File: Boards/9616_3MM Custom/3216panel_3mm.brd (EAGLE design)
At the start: 384.8 x 81.3 mm, 452 parts, among them U1 74HC164D, U10 74HCT04D, U11 HT1632C, U12 HT1632C, U13 74HC164D, U14 HT1632C, U15 HT1632C, U16 74HCT04D, U17 HT1632C, U18 HT1632C, U2 HT1632C, U3 HT1632C, U4 74HCT04D, U5 HT1632C, U6 HT1632C, U7 74HC164D, U8 HT1632C, U9 HT1632C

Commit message: Finished routing board (for Sierra Circuits/PCBCart.com specs)
Signed-off-by: Evan Richardson <erichardson@savi.com>
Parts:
- C1, C2: value 10pf -> 10pF
- moved C5 8.89 mm to (44.2, -14.0)
- moved U6 7.62 mm to (56.7, -16.0)
- moved BR1 7.17 mm to (27.2, -14.7)
- moved R268 0.51 mm to (290.1, 7.62)
- moved R293 0.25 mm to (275.8, -7.62)
- moved R273 0.13 mm to (275.9, 7.62)
- moved R276 0.13 mm to (260.6, 7.62)
- moved R100 0.07 mm to (2.02, -24.1)
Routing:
- net +5V: track 0.00 -> 1258.6 mm, vias 0 -> 22
- net GND: track 0.00 -> 1226.7 mm, vias 0 -> 36
- net WR_A_OUT: track 0.00 -> 352.8 mm, vias 0 -> 7
- net DATA_A_OUT: track 0.00 -> 333.3 mm, vias 0 -> 10
- net WR_B_OUT: track 0.00 -> 305.6 mm, vias 0 -> 9
- net DATA_B_OUT: track 0.00 -> 288.7 mm, vias 0 -> 6
- net CS4: track 0.00 -> 223.0 mm, vias 0 -> 3
- net CSB_4: track 0.00 -> 198.7 mm, vias 0 -> 2
- net CLK_A_OUT: track 0.00 -> 192.3 mm, vias 0 -> 3
- net CLK_B_OUT: track 0.00 -> 178.3 mm, vias 0 -> 4
- net DATA_C_OUT: track 0.00 -> 160.4 mm, vias 0 -> 4
- net WR_C_OUT: track 0.00 -> 154.7 mm, vias 0 -> 7
- net ANODE_J4: track 0.00 -> 124.9 mm, vias 0 -> 1
- net ANODE_D6: track 0.00 -> 109.8 mm, vias 0 -> 1
- net CATHODE_F23: track 0.00 -> 101.9 mm, vias 0 -> 1
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- added copper zone on layer 1, net GND
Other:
- board size 384.8 x 81.3 mm -> 384.5 x 81.3 mm

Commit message: added fiducial marks increased 5V supply to 16mil
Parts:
- added JP1, JP2, JP3, JP4: FIDUCIAL1X2.5, SparkFun-Aesthetics:FIDUCIAL-1X2.5
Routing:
- net CATHODE_A10: track 28.3 -> 29.5 mm
- net CATHODE_A23: track 38.0 -> 39.1 mm
- net CATHODE_J16: track 44.9 -> 45.9 mm
- net CATHODE_A11: track 32.9 -> 33.9 mm
- added copper zone on layer 1, net +5V
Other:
- board size 384.5 x 81.3 mm -> 384.8 x 81.3 mm

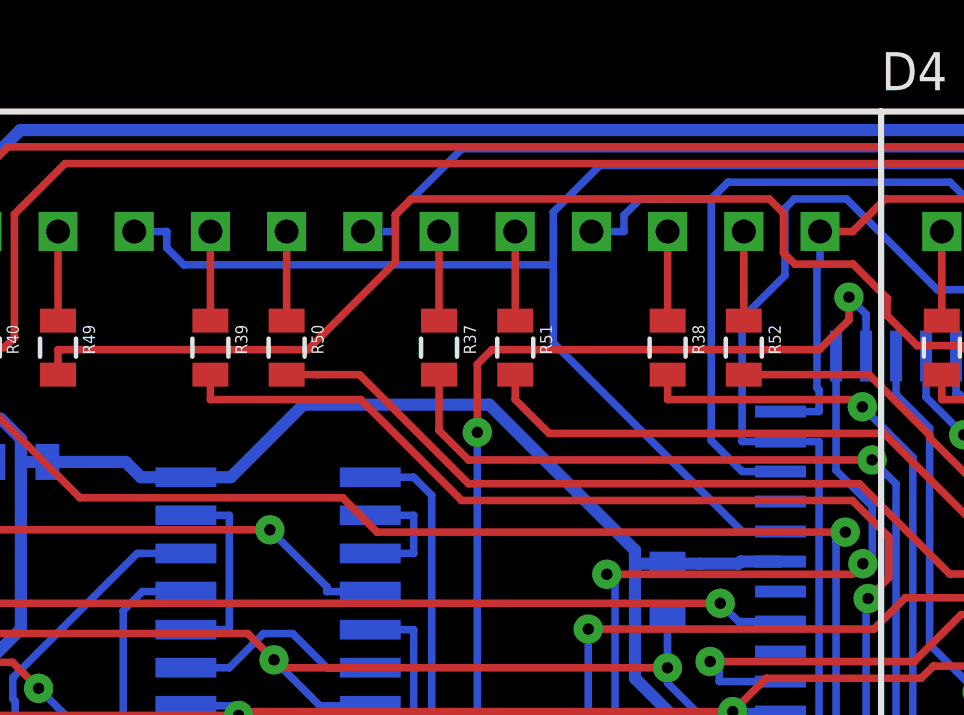
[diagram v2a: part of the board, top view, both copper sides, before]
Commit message: fixed missing connection on pin 19 of 3rd/4th top displays on left side of Boards/9616_3MM Custom/3216panel_3mm.brd
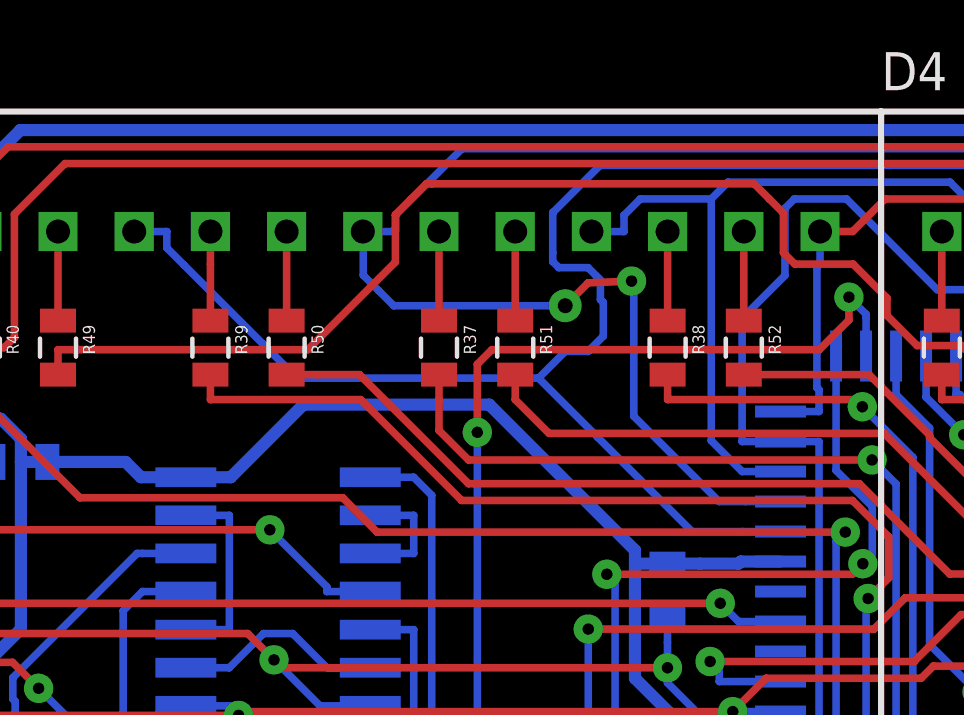
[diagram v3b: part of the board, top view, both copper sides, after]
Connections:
- net ANODE_B1: now also U2.23
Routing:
- net ANODE_B1: track 34.9 -> 56.7 mm, vias 0 -> 2
- net ANODE_B0: track 49.2 -> 54.1 mm
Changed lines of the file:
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@@
 <layer number="17" name="Pads" color="2" fill="1" visible="yes" active="yes"/>
 <layer number="18" name="Vias" color="2" fill="1" visible="yes" active="yes"/>
-<layer number="19" name="Unrouted" color="6" fill="1" visible="yes" active="yes"/>
+<layer number="19" name="Unrouted" color="17" fill="1" visible="yes" active="yes"/>
 <layer number="20" name="Dimension" color="15" fill="1" visible="yes" active="yes"/>
 <layer number="21" name="tPlace" color="7" fill="1" visible="yes" active="yes"/>
@@
 <classes>
 <class number="0" name="default" width="0.254" drill="0.254">
-<clearance class="0" value="0.1524"/>
+<clearance class="0" value="0.3048"/>
 </class>
-<class number="1" name="+5V" width="0.1524" drill="0.254">
-<clearance class="1" value="0.1524"/>
+<class number="1" name="+5V" width="0.3556" drill="0.254">
+<clearance class="1" value="0.3048"/>
 </class>
-<class number="2" name="GND" width="0.1524" drill="0.254">
-<clearance class="2" value="0.1524"/>
+<class number="2" name="GND" width="0.3048" drill="0.254">
+<clearance class="2" value="0.3048"/>
 </class>
 </classes>
@@
 <contactref element="U2" pad="22"/>
 <wire x1="103.105" y1="28" x2="102.0191" y2="28" width="0.254" layer="16"/>
-<wire x1="85.075" y1="26.8901" x2="85.075" y2="28.6488" width="0.254" layer="16"/>
 <wire x1="85.075" y1="28.6488" x2="86.63" y2="30.2038" width="0.254" layer="16"/>
 <wire x1="86.63" y1="30.2038" x2="100.3536" y2="30.2038" width="0.254" layer="16"/>
 <wire x1="100.3536" y1="30.2038" x2="102.0191" y2="28.5383" width="0.254" layer="16"/>
 <wire x1="102.0191" y1="28.5383" x2="102.0191" y2="28" width="0.254" layer="16"/>
-<wire x1="91.3681" y1="18" x2="85.075" y2="24.2931" width="0.254" layer="16"/>
-<wire x1="85.075" y1="24.2931" x2="85.075" y2="26.8901" width="0.254" layer="16"/>
-<wire x1="85.075" y1="26.8901" x2="72.7578" y2="26.8901" width="0.254" layer="16"/>
 <wire x1="72.7578" y1="26.8901" x2="72.1909" y2="27.457" width="0.254" layer="16"/>
 <wire x1="72.1909" y1="27.457" x2="72.1909" y2="28" width="0.254" layer="16"/>
 <wire x1="92.65" y1="18" x2="91.3681" y2="18" width="0.254" layer="16"/>
 <wire x1="71.105" y1="28" x2="72.1909" y2="28" width="0.254" layer="16"/>
+<wire x1="72.7578" y1="26.8901" x2="75.3909" y2="24.257" width="0.254" layer="16"/>
+<wire x1="85.075" y1="28.6488" x2="85.055" y2="28.6288" width="0.254" layer="16"/>
+<wire x1="85.055" y1="28.6288" x2="85.055" y2="27.295" width="0.254" layer="16"/>
+<wire x1="85.055" y1="27.295" x2="85.055" y2="27" width="0.254" layer="16"/>
+<wire x1="91.3681" y1="18" x2="89.696" y2="18" width="0.254" layer="16"/>
+<wire x1="75.3909" y1="24.257" x2="76.5339" y2="23.114" width="0.254" layer="16"/>
+<wire x1="76.5339" y1="23.114" x2="84.582" y2="23.114" width="0.254" layer="16"/>
+<wire x1="85.055" y1="27" x2="85.258" y2="26.797" width="0.254" layer="16"/>
+<wire x1="85.258" y1="26.797" x2="86.233" y2="26.797" width="0.254" layer="16"/>
+<wire x1="86.233" y1="26.797" x2="86.5" y2="26.53" width="0.254" layer="16"/>
+<wire x1="86.5" y1="26.53" x2="86.58" y2="26.45" width="0.254" layer="16"/>
+<wire x1="89.696" y1="18" x2="86.5505" y2="21.1455" width="0.254" layer="16"/>
+<wire x1="86.5505" y1="21.1455" x2="84.582" y2="23.114" width="0.254" layer="16"/>
+<wire x1="84.582" y1="23.114" x2="85.471" y2="24.003" width="0.254" layer="16"/>
+<wire x1="85.471" y1="24.003" x2="86.233" y2="24.003" width="0.254" layer="16"/>
+<wire x1="86.233" y1="24.003" x2="86.741" y2="24.511" width="0.254" layer="16"/>
+<wire x1="86.741" y1="24.511" x2="86.741" y2="25.634" width="0.254" layer="16"/>
+<wire x1="86.741" y1="25.634" x2="86.645" y2="25.73" width="0.254" layer="16"/>
+<wire x1="86.645" y1="25.73" x2="86.645" y2="26.385" width="0.254" layer="16"/>
+<wire x1="86.645" y1="26.385" x2="86.58" y2="26.45" width="0.254" layer="16"/>
 </signal>
 <signal name="ANODE_B1">
@@
 <wire x1="78.725" y1="28" x2="79.8109" y2="28" width="0.254" layer="16"/>
 <wire x1="110.725" y1="28" x2="109.6391" y2="28" width="0.254" layer="16"/>
+<contactref element="U2" pad="23"/>
+<wire x1="92.65" y1="19" x2="91.49" y2="19" width="0.254" layer="16"/>
+<wire x1="91.49" y1="19" x2="90.601" y2="19" width="0.254" layer="16"/>
+<via x="87.683" y="26.349" extent="1-16" drill="0.381" diameter="0.854"/>
+<wire x1="86.233" y1="26.289" x2="85.471" y2="25.527" width="0.254" layer="1"/>
+<via x="85.471" y="25.527" extent="1-16" drill="0.5"/>
+<wire x1="85.471" y1="25.527" x2="79.756" y2="25.527" width="0.254" layer="16"/>
+<wire x1="79.756" y1="25.527" x2="79.248" y2="26.035" width="0.254" layer="16"/>
+<wire x1="79.248" y1="26.035" x2="78.74" y2="26.543" width="0.254" layer="16"/>
+<wire x1="78.725" y1="28" x2="78.74" y2="27.985" width="0.254" layer="16"/>
+<wire x1="78.74" y1="27.985" x2="78.74" y2="26.543" width="0.254" layer="16"/>
+<wire x1="86.233" y1="26.289" x2="87.683" y2="26.349" width="0.254" layer="1"/>
+<wire x1="87.683" y1="26.349" x2="87.757" y2="26.275" width="0.254" layer="16"/>
+<wire x1="87.757" y1="26.275" x2="87.757" y2="21.844" width="0.254" layer="16"/>
+<wire x1="87.757" y1="21.844" x2="90.601" y2="19" width="0.254" layer="16"/>
 </signal>
 <signal name="ANODE_B2">
@@
 <wire x1="79.811" y1="26.982" x2="79.811" y2="28.56" width="0.254" layer="1"/>
 <wire x1="79.811" y1="28.56" x2="80.337" y2="29.086" width="0.254" layer="1"/>
-<wire x1="80.337" y1="29.086" x2="92.2745" y2="29.086" width="0.254" layer="1"/>
 <wire x1="92.2745" y1="29.086" x2="92.7449" y2="28.6156" width="0.254" layer="1"/>
 <wire x1="92.7449" y1="28.6156" x2="92.7449" y2="27.2942" width="0.254" layer="1"/>
@@
 <wire x1="68.565" y1="23.23" x2="68.565" y2="24.0619" width="0.254" layer="1"/>
 <via x="110.6767" y="20.9477" extent="1-16" drill="0.381" diameter="0.854"/>
+<wire x1="92.2745" y1="29.086" x2="91.7695" y2="29.591" width="0.254" layer="1"/>
+<wire x1="91.7695" y1="29.591" x2="81.026" y2="29.591" width="0.254" layer="1"/>
+<wire x1="80.337" y1="29.086" x2="80.842" y2="29.591" width="0.254" layer="1"/>
+<wire x1="80.842" y1="29.591" x2="81.026" y2="29.591" width="0.254" layer="1"/>
 </signal>
 <signal name="CATHODE_B17">
@@
 </signal>
 </signals>
-<errors>
-</errors>
 </board>
 </drawing>
